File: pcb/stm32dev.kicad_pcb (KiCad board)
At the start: 2 copper layers, 52.1 x 30.5 mm, 36 parts, among them J1 USB_C_Receptacle_USB2.0, J3 Micro_SD_Card_Det, U1 XC6206P332MR, U2 STM32F405RGTx, Y1 8 MHz

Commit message: Hmmmm
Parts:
- added AE1: Antenna_Shield, Connector_Coaxial:U.FL_Molex_MCRF_73412-0110_Vertical, F.Cu at (125.1, 92.7)
- added U3: NRF24L01, Package_DFN_QFN:QFN-20-1EP_4x4mm_P0.5mm_EP2.5x2.5mm, F.Cu at (131.4, 94.0)
- SW1, SW2: footprint Button_Switch_SMD:SW_SPST_TL3342 -> Button_Switch_SMD:SW_Push_1P1T_NO_CK_KMR2
- moved D1 55.1 mm to (187.3, 90.2)
- moved R5 15.7 mm to (134.6, 105.4)
- moved SW2 7.22 mm to (131.4, 99.1)
- moved C2 6.25 mm to (132.1, 105.4)
- moved C7 6.25 mm to (136.5, 95.2), turned to 0 degrees
- moved C4 4.44 mm to (140.3, 104.8)
- moved C9 4.44 mm to (139.1, 104.8)
- moved J2 3.81 mm to (126.4, 104.1)
- moved U2 3.81 mm to (146.7, 97.8)
- moved R1 3.42 mm to (129.5, 105.4)
- moved C10 2.97 mm to (136.5, 96.5)
- moved C11 2.84 mm to (136.5, 104.1)
- moved Y1 2.84 mm to (136.5, 100.3)
- moved SW1 1.48 mm to (131.4, 102.9)
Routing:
- net +3V3: track 180.5 -> 0.00 mm, vias 6 -> 0
- net PA12: track 45.8 -> 0.00 mm, vias 2 -> 1
- net PA11: track 43.2 -> 0.00 mm, vias 2 -> 1
- net SWDIO: track 37.1 -> 0.00 mm, vias 1 -> 0
- net SWCLK: track 33.8 -> 0.00 mm, vias 2 -> 0
- net PC6: track 32.4 -> 0.00 mm, vias 2 -> 1
- net SD_DET: track 31.1 -> 0.00 mm, vias 1 -> 0
- net PC13: track 31.0 -> 0.00 mm, vias 2 -> 1
- net SD_D1: track 29.3 -> 0.00 mm, vias 1 -> 0
- net SWO: track 26.4 -> 0.00 mm, vias 1 -> 0
- net NRST: track 26.3 -> 0.00 mm
- net PB9: track 26.1 -> 0.00 mm
- net PC0: track 25.9 -> 0.00 mm
- net PB10: track 25.5 -> 0.00 mm
- net PA10: track 25.1 -> 0.00 mm
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
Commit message: Hmmm
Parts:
- added C14: 20pF, Capacitor_SMD:C_0402_1005Metric, F.Cu at (137.2, 74.3)
- added C15: 20pF, Capacitor_SMD:C_0402_1005Metric, F.Cu at (134.8, 78.3)
- added C16: 1.5pF, Capacitor_SMD:C_0402_1005Metric, F.Cu at (137.2, 76.3)
- added C17: 1pF, Capacitor_SMD:C_0402_1005Metric, F.Cu at (137.7, 78.2)
- added L1: 8.2nH, Inductor_SMD:L_0402_1005Metric, F.Cu at (129.0, 78.8)
- added L2: 2.7nH, Inductor_SMD:L_0402_1005Metric, F.Cu at (134.3, 74.3)
- added L3: 3.9nH, Inductor_SMD:L_0402_1005Metric, F.Cu at (131.9, 78.8)
- added R10: 1M, Resistor_SMD:R_0402_1005Metric, F.Cu at (134.3, 76.3)
- added Y2: 16MHz, Crystal:Crystal_SMD_3225-4Pin_3.2x2.5mm, F.Cu at (130.2, 75.5)
- AE1: footprint Connector_Coaxial:U.FL_Molex_MCRF_73412-0110_Vertical -> Connector_Coaxial:U.FL_Hirose_U.FL-R-SMT-1_Vertical
- J1: moved to F.Cu
- moved D1 28.7 mm to (158.8, 92.7), turned to 180 degrees
- moved R7 10.0 mm to (163.8, 94.6), turned to 180 degrees
- moved R8 9.38 mm to (163.8, 99.7), turned to 180 degrees
- moved R3 8.28 mm to (163.8, 97.2), turned to 180 degrees
- moved R4 8.28 mm to (163.8, 98.4), turned to 180 degrees
- moved R2 8.28 mm to (163.8, 95.9), turned to 180 degrees
- moved D2 6.48 mm to (166.4, 104.8), turned to 0 degrees
- moved C12 4.84 mm to (154.9, 101.6)
- moved C1 4.49 mm to (159.4, 97.2)
- moved U1 4.49 mm to (159.4, 100.3)
- moved C3 4.49 mm to (159.4, 103.5)
- moved C5 4.02 mm to (154.9, 98.4)
- moved C13 2.72 mm to (152.4, 90.8), turned to 90 degrees
- moved J1 1.27 mm to (170.8, 97.8), turned to 90 degrees
- moved C6 0.64 mm to (150.5, 90.2), turned to 0 degrees
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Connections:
- AE1 pad 2: Net-(AE1-Pad2) -> GND
- U3 pad 14: Net-(U3-Pad14) -> GND
- U3 pad 15: Net-(U3-Pad15) -> +3V3
- U3 pad 17: Net-(U3-Pad17) -> GND
- U3 pad 18: Net-(U3-Pad18) -> +3V3
- U3 pad 20: Net-(U3-Pad20) -> GND
- U3 pad 7: Net-(U3-Pad7) -> +3V3
- U3 pad 8: Net-(U3-Pad8) -> GND
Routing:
- net SD_D0: vias 1 -> 0
- net PC6: vias 1 -> 0
- net PC13: vias 1 -> 0
- net PA12: vias 1 -> 0
- net PA11: vias 1 -> 0
- net PA10: vias 1 -> 0

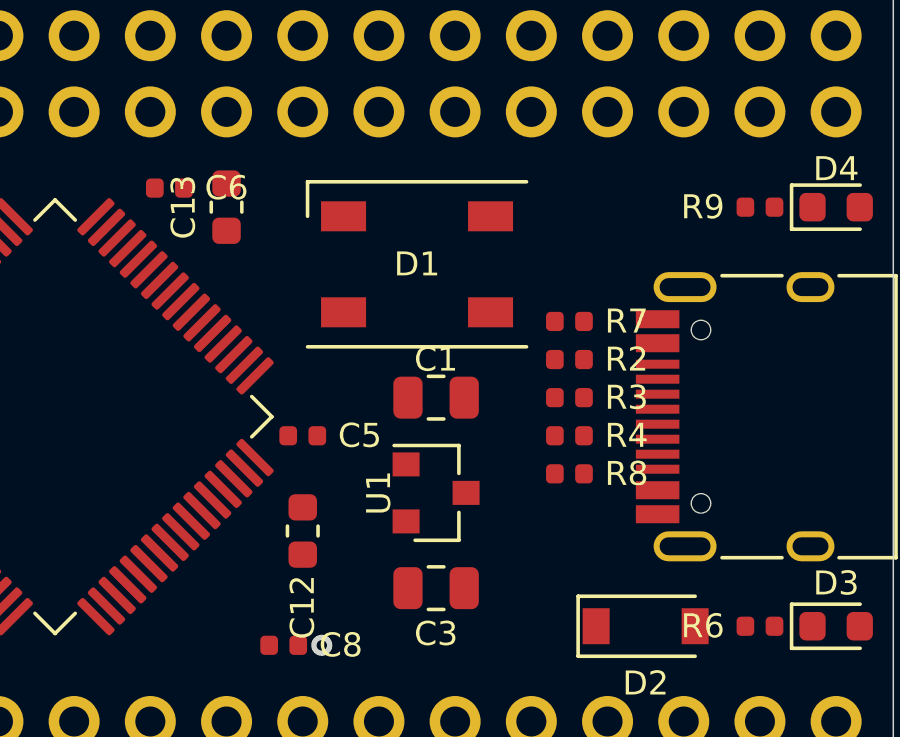
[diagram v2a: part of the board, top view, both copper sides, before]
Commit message: Added sd example
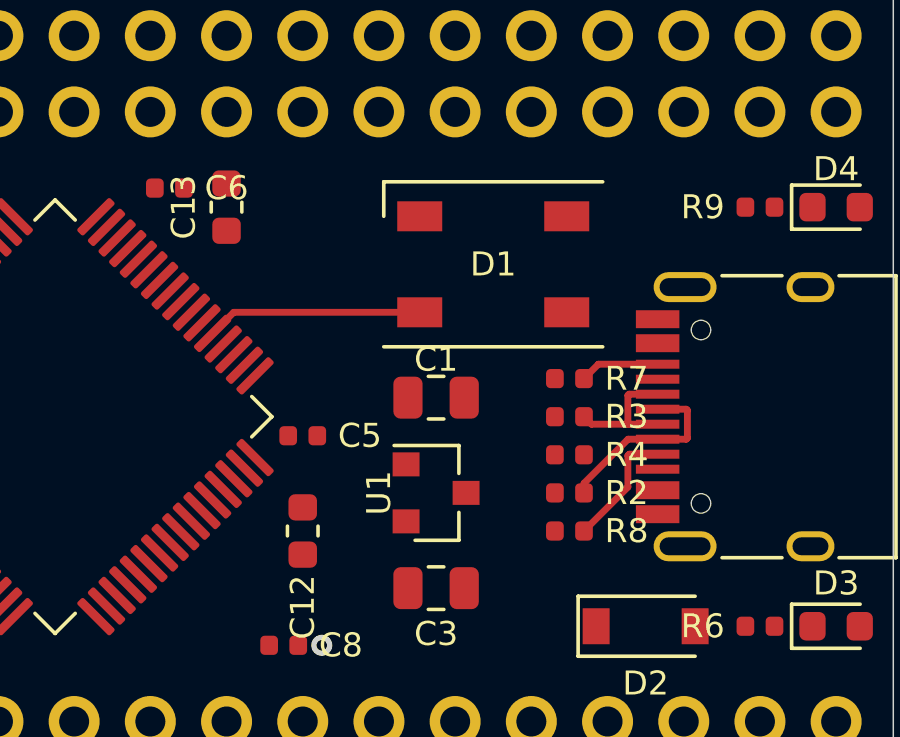
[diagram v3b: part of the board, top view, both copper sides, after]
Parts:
- moved R2 4.44 mm to (163.8, 100.3)
- moved D1 2.54 mm to (161.3, 92.7)
- moved R7 1.91 mm to (163.8, 96.5)
- moved R8 1.91 mm to (163.8, 101.6)
- moved R3 0.64 mm to (163.8, 97.8)
- moved R4 0.64 mm to (163.8, 99.1)
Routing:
- net PC6: track 0.00 -> 7.20 mm
- net Net-(J1-PadA7): track 0.00 -> 6.32 mm
- net Net-(J1-PadA6): track 0.00 -> 4.54 mm
- net Net-(J1-PadA5): track 0.00 -> 4.13 mm
- net Net-(J1-PadB5): track 0.00 -> 2.65 mm

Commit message: Cleaned up old code
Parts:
- moved C17 20.1 mm to (127.0, 95.2), turned to 270 degrees
- moved Y2 17.4 mm to (137.2, 91.4)
- moved C16 16.9 mm to (127.6, 90.2), turned to 180 degrees
- moved C14 16.8 mm to (140.3, 90.8), turned to 270 degrees
- moved C15 12.6 mm to (134.0, 90.8), turned to 90 degrees
- moved L1 11.7 mm to (131.4, 90.2)
- moved L3 11.7 mm to (129.5, 90.2), turned to 180 degrees
- turned U3 to 90 degrees

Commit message: Hmmmm
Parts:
- moved L2 6.19 mm to (129.4, 78.1)

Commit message: Hmmm
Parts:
- Y1: value 8 MHz -> 16MHz; footprint Crystal:Crystal_SMD_Abracon_ABM3-2Pin_5.0x3.2mm -> Crystal:Crystal_SMD_3225-4Pin_3.2x2.5mm
- moved C4 30.1 mm to (167.0, 90.8), turned to 0 degrees
- moved Y1 2.62 mm to (137.2, 102.9), turned to 0 degrees
- moved C9 1.27 mm to (140.3, 104.8)
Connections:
- Y1 pad 1: Net-(C10-Pad1) -> Net-(C11-Pad1)
- Y1 pad 2: Net-(C11-Pad1) -> GND

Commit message: Hmmm
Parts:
- removed R4: 1.5k, Resistor_SMD:R_0402_1005Metric
- removed R5: NM, Resistor_SMD:R_0402_1005Metric
- added JP1: ~, Jumper:SolderJumper-3_P1.3mm_Bridged2Bar12_Pad1.0x1.5mm, B.Cu at (162.6, 90.8)
- AE1: value Antenna_Shield -> ~
- R1: value NM -> 10k
- moved R1 31.0 mm to (156.8, 90.8), turned to 270 degrees
- moved C2 9.94 mm to (136.5, 96.5), turned to 0 degrees
- moved Y1 2.01 mm to (136.5, 101.0), turned to 90 degrees
- moved C9 1.42 mm to (141.6, 104.1), turned to 180 degrees
- moved C10 1.27 mm to (136.5, 97.8)
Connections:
- C4 pad 1: +3V3 -> Net-(C4-Pad1)
- D1 pad 1: +3V3 -> Net-(C4-Pad1)
- R1 pad 1: +3V3 -> Net-(C4-Pad1)
- R1 pad 2: NRST -> PC6
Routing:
- net +3V3: track 0.00 -> 23.6 mm
- net PC0: track 0.00 -> 20.7 mm
- net PC1: track 0.00 -> 18.3 mm
- net PC2: track 0.00 -> 16.0 mm
- net PC3: track 0.00 -> 13.7 mm
- net VBUS: track 0.00 -> 13.0 mm
- net PA0: track 0.00 -> 11.7 mm
- net PA1: track 0.00 -> 9.40 mm
- net Net-(C10-Pad1): track 0.00 -> 8.72 mm
- net PA3: track 0.00 -> 7.39 mm
- net PA2: track 0.00 -> 7.31 mm
- net Net-(C11-Pad1): track 0.00 -> 7.11 mm
- added copper zone on B.Cu, net BO0
- added copper zone on F.Cu, net BO0
- removed copper zone on B.Cu, net GND
- removed copper zone on F.Cu, net GND

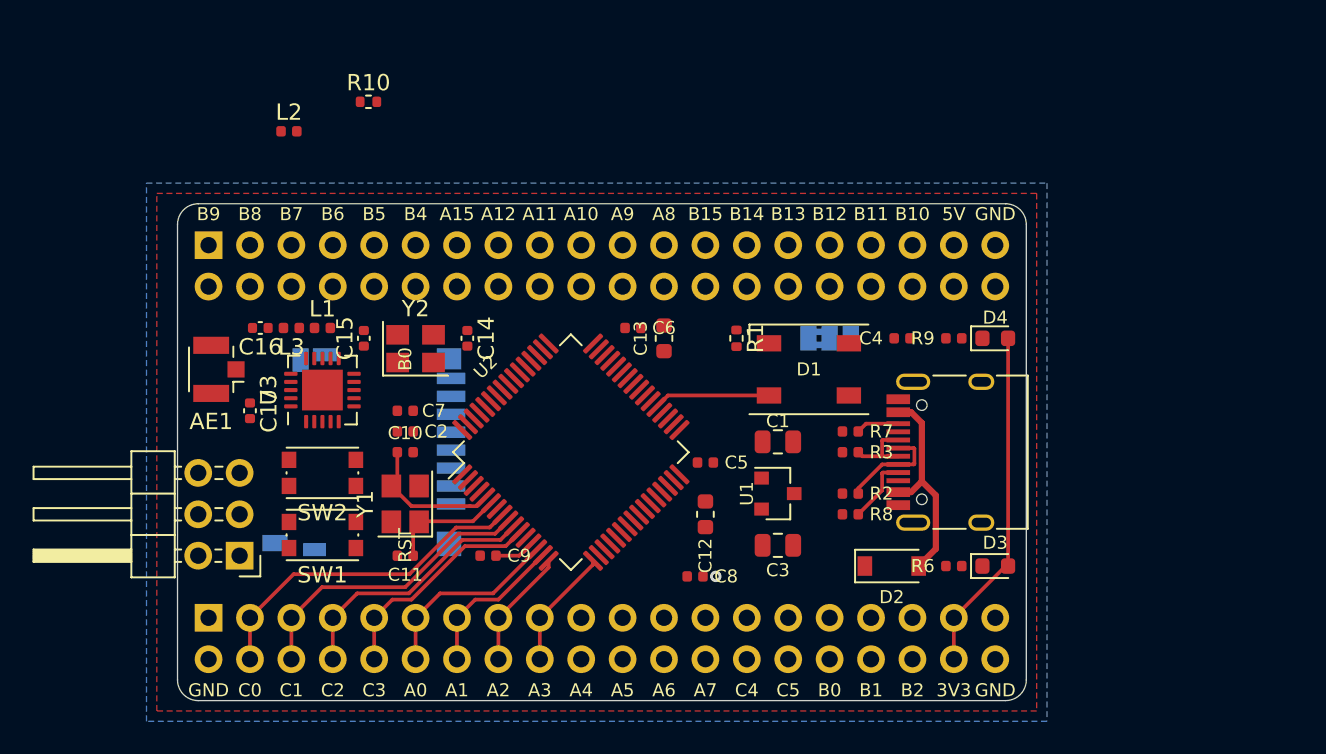
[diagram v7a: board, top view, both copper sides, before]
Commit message: Removed all the wireless stuff - back to rev b
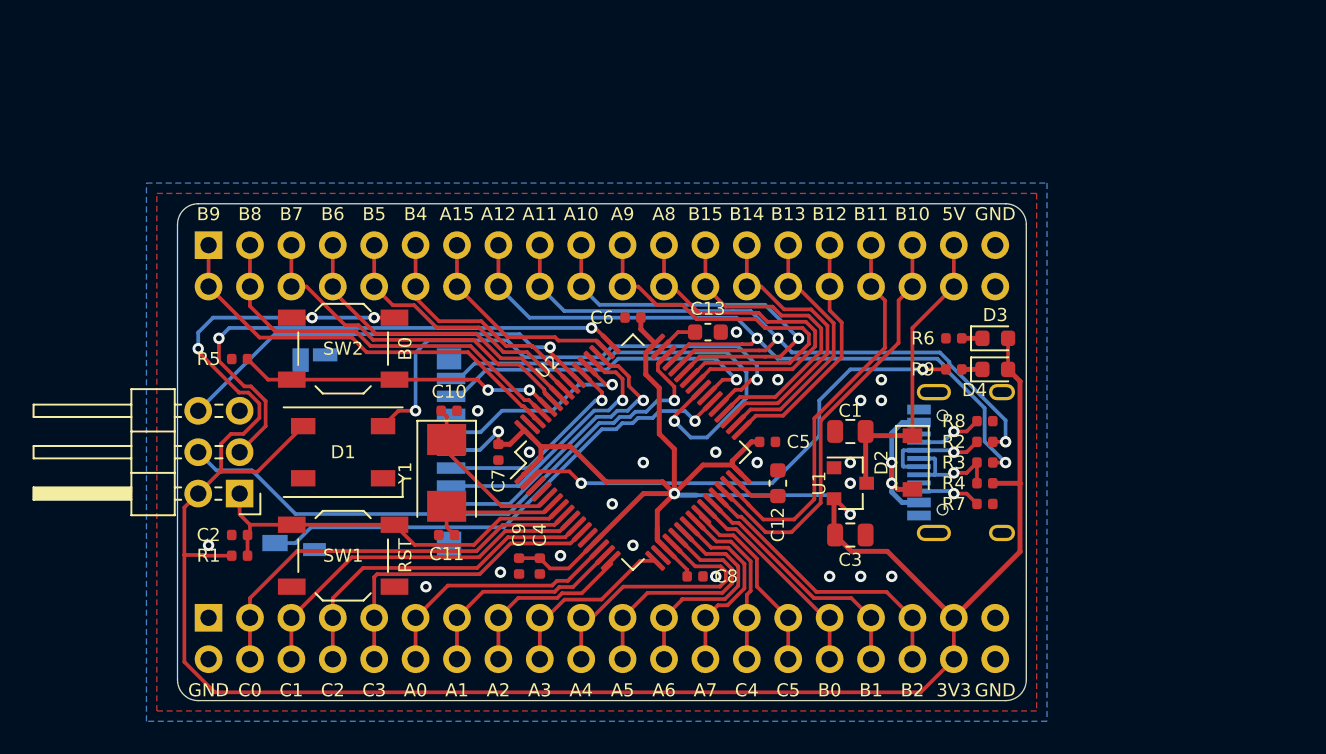
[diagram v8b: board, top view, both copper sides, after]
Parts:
- removed AE1: ~, Connector_Coaxial:U.FL_Hirose_U.FL-R-SMT-1_Vertical
- removed C14, C15: 20pF, Capacitor_SMD:C_0402_1005Metric
- removed C16: 1.5pF, Capacitor_SMD:C_0402_1005Metric
- removed C17: 1pF, Capacitor_SMD:C_0402_1005Metric
- removed JP1: ~, Jumper:SolderJumper-3_P1.3mm_Bridged2Bar12_Pad1.0x1.5mm
- removed L1: 8.2nH, Inductor_SMD:L_0402_1005Metric
- removed L2: 2.7nH, Inductor_SMD:L_0402_1005Metric
- removed L3: 3.9nH, Inductor_SMD:L_0402_1005Metric
- removed R10: 1M, Resistor_SMD:R_0402_1005Metric
- removed U3: NRF24L01, Package_DFN_QFN:QFN-20-1EP_4x4mm_P0.5mm_EP2.5x2.5mm
- removed Y2: 16MHz, Crystal:Crystal_SMD_3225-4Pin_3.2x2.5mm
- added R4: 1.5k, Resistor_SMD:R_0402_1005Metric, F.Cu at (172.1, 99.7)
- added R5: NM, Resistor_SMD:R_0402_1005Metric, F.Cu at (126.4, 92.1)
- J1: moved to B.Cu
- R1: value 10k -> NM
- SW1, SW2: footprint Button_Switch_SMD:SW_Push_1P1T_NO_CK_KMR2 -> Button_Switch_SMD:SW_SPST_TL3342
- Y1: value 16MHz -> 8 MHz; footprint Crystal:Crystal_SMD_3225-4Pin_3.2x2.5mm -> Crystal:Crystal_SMD_Abracon_ABM3-2Pin_5.0x3.2mm
- moved R1 33.3 mm to (126.4, 104.1), turned to 0 degrees
- moved D1 29.0 mm to (132.7, 97.8), turned to 0 degrees
- moved C4 26.3 mm to (144.8, 104.8), turned to 270 degrees
- moved D3 14.0 mm to (172.7, 90.8)
- moved R6 14.0 mm to (170.2, 90.8)
- moved C2 12.0 mm to (126.4, 102.9), turned to 180 degrees
- moved R8 10.0 mm to (172.1, 95.9), turned to 0 degrees
- moved R7 9.38 mm to (172.1, 101.0), turned to 0 degrees
- moved R2 8.84 mm to (172.1, 97.2), turned to 0 degrees
- moved R3 8.28 mm to (172.1, 98.4), turned to 0 degrees
- moved SW2 7.73 mm to (132.7, 91.4)
- moved D2 6.48 mm to (167.6, 98.4), turned to 270 degrees
- moved C7 6.25 mm to (142.2, 97.8), turned to 270 degrees
- moved C12 4.84 mm to (159.4, 99.7)
- moved C1 4.49 mm to (163.8, 96.5)
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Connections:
- C4 pad 1: Net-(C4-Pad1) -> +3V3
- D1 pad 1: Net-(C4-Pad1) -> +3V3
- R1 pad 1: Net-(C4-Pad1) -> +3V3
- R1 pad 2: PC6 -> NRST
- Y1 pad 1: Net-(C11-Pad1) -> Net-(C10-Pad1)
- Y1 pad 2: GND -> Net-(C11-Pad1)
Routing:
- net +3V3: track 23.6 -> 202.7 mm, vias 0 -> 6
- net PA12: track 0.00 -> 46.0 mm, vias 0 -> 2
- net PA11: track 0.00 -> 43.5 mm, vias 0 -> 2
- net SWDIO: track 0.00 -> 37.1 mm, vias 0 -> 1
- net SWCLK: track 0.00 -> 33.8 mm, vias 0 -> 2
- net SD_DET: track 0.00 -> 31.1 mm, vias 0 -> 1
- net PC13: track 0.00 -> 30.2 mm, vias 0 -> 2
- net SD_D1: track 0.00 -> 29.3 mm, vias 0 -> 1
- net SWO: track 0.00 -> 26.4 mm, vias 0 -> 1
- net PB9: track 0.00 -> 26.1 mm
- net PB10: track 0.00 -> 25.8 mm
- net PC6: track 7.20 -> 32.4 mm, vias 0 -> 2
- net PA10: track 0.00 -> 25.1 mm, vias 0 -> 1
- net NRST: track 0.00 -> 24.5 mm
- net PB8: track 0.00 -> 24.3 mm
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- added copper zone on B.Cu, net GND
- added copper zone on F.Cu, net GND
- removed copper zone on B.Cu, net BO0
- removed copper zone on F.Cu, net BO0
